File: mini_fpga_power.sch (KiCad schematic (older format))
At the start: 44 parts, among them J1 PWR_HEADER1X6, U1 AP7331, U2 PAM2306D, U3 XC6SLX9

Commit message: minor netlist changes
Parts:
- added R?: 40k1%, ~, symbol R
- R1: value 380k1% -> 340k1%
- gave numbers to parts that had none: 2
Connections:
- net at C4.2, R2.1, U2.4 (FB1): now also R?.2; no longer R1.2
- new net: R1.2, R?.1
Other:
- moved on the sheet: R1
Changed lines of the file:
@@
 Sheet 2 6
 Title ""
-Date "30 jul 2014"
+Date "2 aug 2014"
 Rev ""
 Comp ""
@@
 $EndComp
 $Comp
-L GND #PWR01
+L GND #PWR28
 U 1 1 53CA8335
 P 9450 4650
-F 0 "#PWR01" H 9450 4650 30  0001 C CNN
+F 0 "#PWR28" H 9450 4650 30  0001 C CNN
 F 1 "GND" H 9450 4580 30  0001 C CNN
 F 2 "" H 9450 4650 60  0000 C CNN
@@
 $EndComp
 $Comp
-L GND #PWR02
+L GND #PWR23
 U 1 1 53C9E69C
 P 6200 2850
-F 0 "#PWR02" H 6200 2850 30  0001 C CNN
+F 0 "#PWR23" H 6200 2850 30  0001 C CNN
 F 1 "GND" H 6200 2780 30  0001 C CNN
 F 2 "" H 6200 2850 60  0000 C CNN
@@
 $EndComp
 $Comp
-L GND #PWR03
+L GND #PWR21
 U 1 1 53C9E6A9
 P 6200 2050
-F 0 "#PWR03" H 6200 2050 30  0001 C CNN
+F 0 "#PWR21" H 6200 2050 30  0001 C CNN
 F 1 "GND" H 6200 1980 30  0001 C CNN
 F 2 "" H 6200 2050 60  0000 C CNN
@@
 $EndComp
 $Comp
-L GND #PWR04
+L GND #PWR19
 U 1 1 53C9EA76
 P 6100 5300
-F 0 "#PWR04" H 6100 5300 30  0001 C CNN
+F 0 "#PWR19" H 6100 5300 30  0001 C CNN
 F 1 "GND" H 6100 5230 30  0001 C CNN
 F 2 "" H 6100 5300 60  0000 C CNN
@@
 $EndComp
 $Comp
-L +3.3V #PWR05
+L +3.3V #PWR20
 U 1 1 53CC5510
 P 6200 1550
-F 0 "#PWR05" H 6200 1510 30  0001 C CNN
+F 0 "#PWR20" H 6200 1510 30  0001 C CNN
 F 1 "+3.3V" H 6200 1660 30  0000 C CNN
 F 2 "" H 6200 1550 60  0000 C CNN
@@
 $EndComp
 $Comp
-L +3.3V #PWR06
+L +3.3V #PWR24
 U 1 1 53CC551D
 P 6200 3250
-F 0 "#PWR06" H 6200 3210 30  0001 C CNN
+F 0 "#PWR24" H 6200 3210 30  0001 C CNN
 F 1 "+3.3V" H 6200 3360 30  0000 C CNN
 F 2 "" H 6200 3250 60  0000 C CNN
@@
 $EndComp
 $Comp
-L +3.3V #PWR07
+L +3.3V #PWR25
 U 1 1 53CC5523
 P 6200 3850
-F 0 "#PWR07" H 6200 3810 30  0001 C CNN
+F 0 "#PWR25" H 6200 3810 30  0001 C CNN
 F 1 "+3.3V" H 6200 3960 30  0000 C CNN
 F 2 "" H 6200 3850 60  0000 C CNN
@@
 $EndComp
 $Comp
-L +3.3V #PWR08
+L +3.3V #PWR26
 U 1 1 53CC5529
 P 6200 4350
-F 0 "#PWR08" H 6200 4310 30  0001 C CNN
+F 0 "#PWR26" H 6200 4310 30  0001 C CNN
 F 1 "+3.3V" H 6200 4460 30  0000 C CNN
 F 2 "" H 6200 4350 60  0000 C CNN
@@
 $EndComp
 $Comp
-L +5V #PWR09
+L +5V #PWR3
 U 1 1 53CC8C3E
 P 1700 1650
-F 0 "#PWR09" H 1700 1740 20  0001 C CNN
+F 0 "#PWR3" H 1700 1740 20  0001 C CNN
 F 1 "+5V" H 1700 1740 30  0000 C CNN
 F 2 "" H 1700 1650 60  0000 C CNN
@@
 $EndComp
 $Comp
-L GND #PWR010
+L GND #PWR2
 U 1 1 53CC8D32
 P 1400 2700
-F 0 "#PWR010" H 1400 2700 30  0001 C CNN
+F 0 "#PWR2" H 1400 2700 30  0001 C CNN
 F 1 "GND" H 1400 2630 30  0001 C CNN
 F 2 "" H 1400 2700 60  0000 C CNN
@@
 $EndComp
 $Comp
-L +5V #PWR011
+L +5V #PWR15
 U 1 1 53CC8F28
 P 3600 1650
-F 0 "#PWR011" H 3600 1740 20  0001 C CNN
+F 0 "#PWR15" H 3600 1740 20  0001 C CNN
 F 1 "+5V" H 3600 1740 30  0000 C CNN
 F 2 "" H 3600 1650 60  0000 C CNN
@@
 $EndComp
 $Comp
-L GND #PWR012
+L GND #PWR16
 U 1 1 53CC8F2E
 P 3950 2700
-F 0 "#PWR012" H 3950 2700 30  0001 C CNN
+F 0 "#PWR16" H 3950 2700 30  0001 C CNN
 F 1 "GND" H 3950 2630 30  0001 C CNN
 F 2 "" H 3950 2700 60  0000 C CNN
@@
 L R R1
 U 1 1 53D05EFE
-P 2200 3500
-F 0 "R1" V 2280 3500 40  0000 C CNN
-F 1 "380k1%" V 2207 3501 40  0000 C CNN
-F 2 "~" V 2130 3500 30  0000 C CNN
-F 3 "~" H 2200 3500 30  0000 C CNN
-	1    2200 3500
+P 2850 3600
+F 0 "R1" V 2930 3600 40  0000 C CNN
+F 1 "340k1%" V 2857 3601 40  0000 C CNN
+F 2 "~" V 2780 3600 30  0000 C CNN
+F 3 "~" H 2850 3600 30  0000 C CNN
+	1    2850 3600
 	1    0    0    -1
 $EndComp
@@
 $EndComp
 $Comp
-L GND #PWR013
+L GND #PWR8
 U 1 1 53D06303
 P 2200 4600
-F 0 "#PWR013" H 2200 4600 30  0001 C CNN
+F 0 "#PWR8" H 2200 4600 30  0001 C CNN
 F 1 "GND" H 2200 4530 30  0001 C CNN
 F 2 "" H 2200 4600 60  0000 C CNN
@@
 $EndComp
 $Comp
-L GND #PWR014
+L GND #PWR5
 U 1 1 53D071D6
 P 1750 7000
-F 0 "#PWR014" H 1750 7000 30  0001 C CNN
+F 0 "#PWR5" H 1750 7000 30  0001 C CNN
 F 1 "GND" H 1750 6930 30  0001 C CNN
 F 2 "" H 1750 7000 60  0000 C CNN
@@
 $EndComp
 $Comp
-L GND #PWR015
+L GND #PWR14
 U 1 1 53D07B12
 P 3450 7600
-F 0 "#PWR015" H 3450 7600 30  0001 C CNN
+F 0 "#PWR14" H 3450 7600 30  0001 C CNN
 F 1 "GND" H 3450 7530 30  0001 C CNN
 F 2 "" H 3450 7600 60  0000 C CNN
@@
 $EndComp
 $Comp
-L +3.3V #PWR016
+L +3.3V #PWR17
 U 1 1 53D59E10
 P 4450 750
-F 0 "#PWR016" H 4450 710 30  0001 C CNN
+F 0 "#PWR17" H 4450 710 30  0001 C CNN
 F 1 "+3.3V" H 4450 860 30  0000 C CNN
 F 2 "" H 4450 750 60  0000 C CNN
@@
 $EndComp
 $Comp
-L +2.5V #PWR017
+L +2.5V #PWR4
 U 1 1 53D59E1F
 P 1700 3150
-F 0 "#PWR017" H 1700 3100 20  0001 C CNN
+F 0 "#PWR4" H 1700 3100 20  0001 C CNN
 F 1 "+2.5V" H 1700 3250 30  0000 C CNN
 F 2 "" H 1700 3150 60  0000 C CNN
@@
 $EndComp
 $Comp
-L +5V #PWR018
+L +5V #PWR10
 U 1 1 53D59E2C
 P 2350 4850
-F 0 "#PWR018" H 2350 4940 20  0001 C CNN
+F 0 "#PWR10" H 2350 4940 20  0001 C CNN
 F 1 "+5V" H 2350 4940 30  0000 C CNN
 F 2 "" H 2350 4850 60  0000 C CNN
@@
 $EndComp
 $Comp
-L +2.5V #PWR019
+L +2.5V #PWR9
 U 1 1 53D59E32
 P 2250 4950
-F 0 "#PWR019" H 2250 4900 20  0001 C CNN
+F 0 "#PWR9" H 2250 4900 20  0001 C CNN
 F 1 "+2.5V" H 2250 5050 30  0000 C CNN
 F 2 "" H 2250 4950 60  0000 C CNN
@@
 $EndComp
 $Comp
-L +3.3V #PWR020
+L +3.3V #PWR7
 U 1 1 53D59E38
 P 2150 5050
-F 0 "#PWR020" H 2150 5010 30  0001 C CNN
+F 0 "#PWR7" H 2150 5010 30  0001 C CNN
 F 1 "+3.3V" H 2150 5160 30  0000 C CNN
 F 2 "" H 2150 5050 60  0000 C CNN
@@
 $EndComp
 $Comp
-L GND #PWR021
+L GND #PWR11
 U 1 1 53D59E44
 P 3250 5700
-F 0 "#PWR021" H 3250 5700 30  0001 C CNN
+F 0 "#PWR11" H 3250 5700 30  0001 C CNN
 F 1 "GND" H 3250 5630 30  0001 C CNN
 F 2 "" H 3250 5700 60  0000 C CNN
@@
 $EndComp
 $Comp
-L +3.3V #PWR022
+L +3.3V #PWR1
 U 1 1 53D5A438
 P 1200 5900
-F 0 "#PWR022" H 1200 5860 30  0001 C CNN
+F 0 "#PWR1" H 1200 5860 30  0001 C CNN
 F 1 "+3.3V" H 1200 6010 30  0000 C CNN
 F 2 "" H 1200 5900 60  0000 C CNN
@@
 $EndComp
 $Comp
-L +3.3V #PWR023
+L +3.3V #PWR12
 U 1 1 53D5A43E
 P 3400 3950
-F 0 "#PWR023" H 3400 3910 30  0001 C CNN
+F 0 "#PWR12" H 3400 3910 30  0001 C CNN
 F 1 "+3.3V" H 3400 4060 30  0000 C CNN
 F 2 "" H 3400 3950 60  0000 C CNN
@@
 $EndComp
 $Comp
-L GND #PWR024
+L GND #PWR18
 U 1 1 53D5A459
 P 5250 4150
-F 0 "#PWR024" H 5250 4150 30  0001 C CNN
+F 0 "#PWR18" H 5250 4150 30  0001 C CNN
 F 1 "GND" H 5250 4080 30  0001 C CNN
 F 2 "" H 5250 4150 60  0000 C CNN
@@
 Power status LED
 $Comp
-L +1.2V #PWR025
+L +1.2V #PWR13
 U 1 1 53D5AB1F
 P 3450 6150
-F 0 "#PWR025" H 3450 6290 20  0001 C CNN
+F 0 "#PWR13" H 3450 6290 20  0001 C CNN
 F 1 "+1.2V" H 3450 6260 30  0000 C CNN
 F 2 "" H 3450 6150 60  0000 C CNN
@@
 $EndComp
 $Comp
-L +1.2V #PWR026
+L +1.2V #PWR6
 U 1 1 53D5AB2C
 P 2050 5150
-F 0 "#PWR026" H 2050 5290 20  0001 C CNN
+F 0 "#PWR6" H 2050 5290 20  0001 C CNN
 F 1 "+1.2V" H 2050 5260 30  0000 C CNN
 F 2 "" H 2050 5150 60  0000 C CNN
@@
 $EndComp
 $Comp
-L +1.2V #PWR027
+L +1.2V #PWR22
 U 1 1 53D5AB32
 P 6200 2350
-F 0 "#PWR027" H 6200 2490 20  0001 C CNN
+F 0 "#PWR22" H 6200 2490 20  0001 C CNN
 F 1 "+1.2V" H 6200 2460 30  0000 C CNN
 F 2 "" H 6200 2350 60  0000 C CNN
@@
 $EndComp
 $Comp
-L +2.5V #PWR028
+L +2.5V #PWR27
 U 1 1 53D78C67
 P 6200 4850
-F 0 "#PWR028" H 6200 4800 20  0001 C CNN
+F 0 "#PWR27" H 6200 4800 20  0001 C CNN
 F 1 "+2.5V" H 6200 4950 30  0000 C CNN
 F 2 "" H 6200 4850 60  0000 C CNN
@@
 $EndComp
 $Comp
-L R R?
+L R R5
 U 1 1 53D869FB
 P 5050 1050
-F 0 "R?" V 5130 1050 40  0000 C CNN
+F 0 "R5" V 5130 1050 40  0000 C CNN
 F 1 "510k .5%" V 5057 1051 40  0000 C CNN
 F 2 "~" V 4980 1050 30  0000 C CNN
@@
 $EndComp
 $Comp
-L R R?
+L R R59
 U 1 1 53D86A01
 P 5050 1650
-F 0 "R?" V 5130 1650 40  0000 C CNN
+F 0 "R59" V 5130 1650 40  0000 C CNN
 F 1 "30k .5%" V 5057 1651 40  0000 C CNN
 F 2 "~" V 4980 1650 30  0000 C CNN
@@
 	2200 3750 2200 3950
 Wire Wire Line
-	2200 3200 2200 3250
+	2200 3200 2200 3350
 Wire Wire Line
 	1700 3200 2550 3200
@@
 	3600 1650 3600 2450
 Wire Wire Line
-	3400 1950 3800 1950
+	3800 1950 3400 1950
 Connection ~ 1700 2450
 Wire Wire Line
@@
 Wire Wire Line
 	9250 2050 9450 2050
+$Comp
+L R R?
+U 1 1 53DC563C
+P 2850 4200
+F 0 "R?" V 2930 4200 40  0000 C CNN
+F 1 "40k1%" V 2857 4201 40  0000 C CNN
+F 2 "~" V 2780 4200 30  0000 C CNN
+F 3 "~" H 2850 4200 30  0000 C CNN
+	1    2850 4200
+	1    0    0    -1
+$EndComp
+Wire Wire Line
+	2850 3950 2850 3850
+Wire Wire Line
+	2200 3350 2850 3350
+Wire Wire Line
+	2200 3750 2300 3750
+Wire Wire Line
+	2300 3750 2300 4450
+Wire Wire Line
+	2300 4450 2850 4450
 $EndSCHEMATC

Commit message: Final state of 2sqin design, going to move to 4sqin to actually be able to complete the design.
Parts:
- gave numbers to parts that had none: 1
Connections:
- net +2.5V: now also J1.4 (+2.5V); no longer J1.3 (+3.3V)
- net +3.3V: now also J1.3 (+3.3V); no longer J1.4 (+2.5V)
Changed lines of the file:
@@
 $EndComp
 $Comp
-L +2.5V #PWR9
-U 1 1 53D59E32
+L +3.3V #PWR7
+U 1 1 53D59E38
 P 2250 4950
-F 0 "#PWR9" H 2250 4900 20  0001 C CNN
-F 1 "+2.5V" H 2250 5050 30  0000 C CNN
+F 0 "#PWR7" H 2250 4910 30  0001 C CNN
+F 1 "+3.3V" H 2250 5060 30  0000 C CNN
 F 2 "" H 2250 4950 60  0000 C CNN
 F 3 "" H 2250 4950 60  0000 C CNN
 	1    2250 4950
-	1    0    0    -1
-$EndComp
-$Comp
-L +3.3V #PWR7
-U 1 1 53D59E38
-P 2150 5050
-F 0 "#PWR7" H 2150 5010 30  0001 C CNN
-F 1 "+3.3V" H 2150 5160 30  0000 C CNN
-F 2 "" H 2150 5050 60  0000 C CNN
-F 3 "" H 2150 5050 60  0000 C CNN
-	1    2150 5050
 	1    0    0    -1
 $EndComp
@@
 	3350 5150 2150 5150
 Wire Wire Line
-	2250 5050 2250 4950
-Wire Wire Line
-	3350 5050 2250 5050
-Wire Wire Line
 	2350 4950 2350 4850
 Wire Wire Line
@@
 	9250 2050 9450 2050
 $Comp
-L R R?
+L R R60
 U 1 1 53DC563C
 P 2850 4200
-F 0 "R?" V 2930 4200 40  0000 C CNN
+F 0 "R60" V 2930 4200 40  0000 C CNN
 F 1 "40k1%" V 2857 4201 40  0000 C CNN
 F 2 "~" V 2780 4200 30  0000 C CNN
@@
 Wire Wire Line
 	2300 4450 2850 4450
+$Comp
+L +2.5V #PWR?
+U 1 1 53DC870F
+P 2150 5050
+F 0 "#PWR?" H 2150 5000 20  0001 C CNN
+F 1 "+2.5V" H 2150 5150 30  0000 C CNN
+F 2 "" H 2150 5050 60  0000 C CNN
+F 3 "" H 2150 5050 60  0000 C CNN
+	1    2150 5050
+	1    0    0    -1
+$EndComp
+Wire Wire Line
+	2250 4950 2250 5050
+Wire Wire Line
+	2250 5050 3350 5050
 $EndSCHEMATC

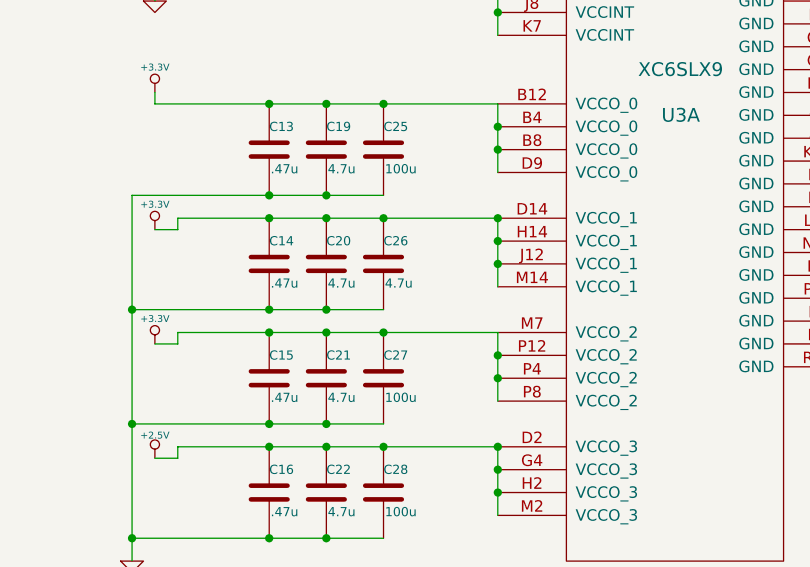
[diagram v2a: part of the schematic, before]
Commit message: Capacitor value error correction.
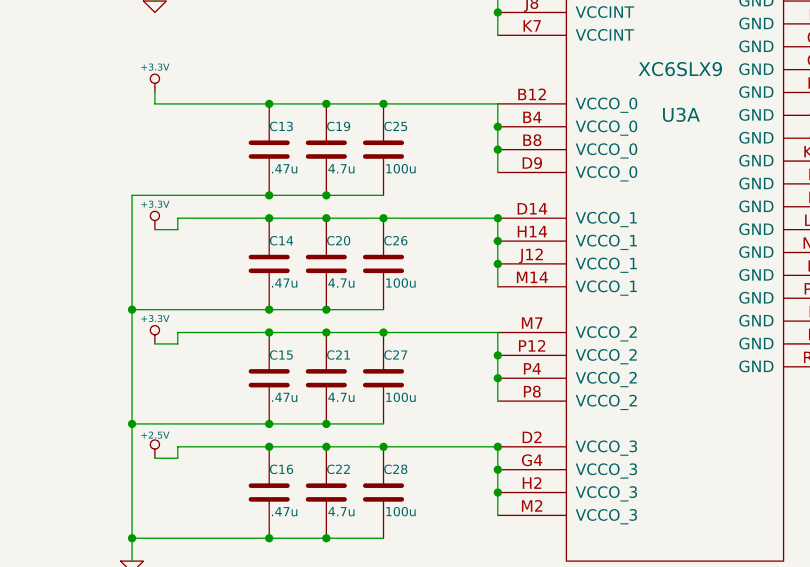
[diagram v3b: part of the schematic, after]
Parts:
- C26: value 4.7u -> 100u
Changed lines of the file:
@@
 Sheet 2 6
 Title ""
-Date "2 aug 2014"
+Date "3 aug 2014"
 Rev ""
 Comp ""
@@
 P 7200 4000
 F 0 "C26" H 7200 4100 40  0000 L CNN
-F 1 "4.7u" H 7206 3915 40  0000 L CNN
+F 1 "100u" H 7206 3915 40  0000 L CNN
 F 2 "~" H 7238 3850 30  0000 C CNN
 F 3 "~" H 7200 4000 60  0000 C CNN
